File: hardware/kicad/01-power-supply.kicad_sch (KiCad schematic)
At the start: 29 parts, among them J1 USB_C, J3 JST PH 2-pin, Q1 SI2301CDS, SW16 SS-12D00G3, U2 IP5306, U3 SY8089AAAC, U4 USBLC6-2SC6

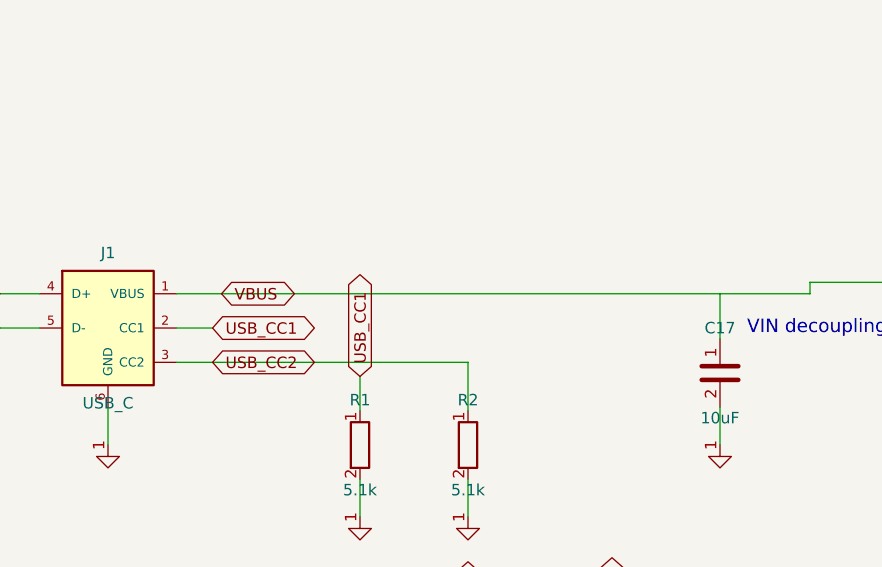
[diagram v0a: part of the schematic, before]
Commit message: feat(hw): EN RC network, fused VBUS input, current-limited backlight — R25 respin trio
Three coordinated design fixes landed together with their full gate,
bench and release integration (work split across two parallel sessions):

- R3 (10k) + C31 (100nF) on EN — the RC the module datasheet p.28
  fig.7 requires (R25-CRIT-1: every board through v4.3.1 shipped
  without it on the strength of a false justification comment).
  EN now solves to the +3V3 rail through the pull-up.
- F1 (PTC resettable fuse 2A 1812, C960026) on the USB input:
  J1 delivers on the new VBUS_IN net and reaches VBUS through F1.
  PWR_FLAG added on the post-fuse rail (J1's power-out pin moved nets).
- R27 (20R 1206) backlight series resistor: LED-A now fed from +5V
  through R27 on the new LED_BLA net (R25-HIGH-1, unbounded current).
  First placement collided with the LCD B.Cu verticals; final position
  (121.7, 45.5) clears the corridor.

Integration completed in this commit:
- verify_polarity: strict expectations for R3/C31/R27/F1, J1 pins moved
  to VBUS_IN, J4.8 backlight expectation moved to LED_BLA — all read
  off the copper.
- vbench corpus: R25-CRIT-1, R10-LOW-7, R25-HIGH-1 flipped from live
  board facts to mutation reinjection (detach R3/C31/R27 must be caught
  by name); R24-HIGH-3 moved to a move_pin drift mutation — the detach
  variant became structurally invisible to the bench once EN gained
  R3/C31 (declared-pad D3 exemption); note records why. usb_cold_boot
  flips its EN assertion exactly as its own text promised; export
  header now derives VB_EN_FLOATING=0; VBUS invariant follows the
  fused chain.
- Gates: R_1206/F_1812 footprints known, F1 value mapping, LED_BLA in
  the Net Explorer section law, schematic caption collisions resolved.
- Release fully synced (gerbers, BOM, CPL, d356, zip, jlcpcb mirror),
  iBOM + schematic SVG/PDF renders + combined PDF regenerated.

Tests: verify-all ALL CHECKS PASSED (incl. polarity 274 checks,
netlist-diff, isolation, e-test on release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
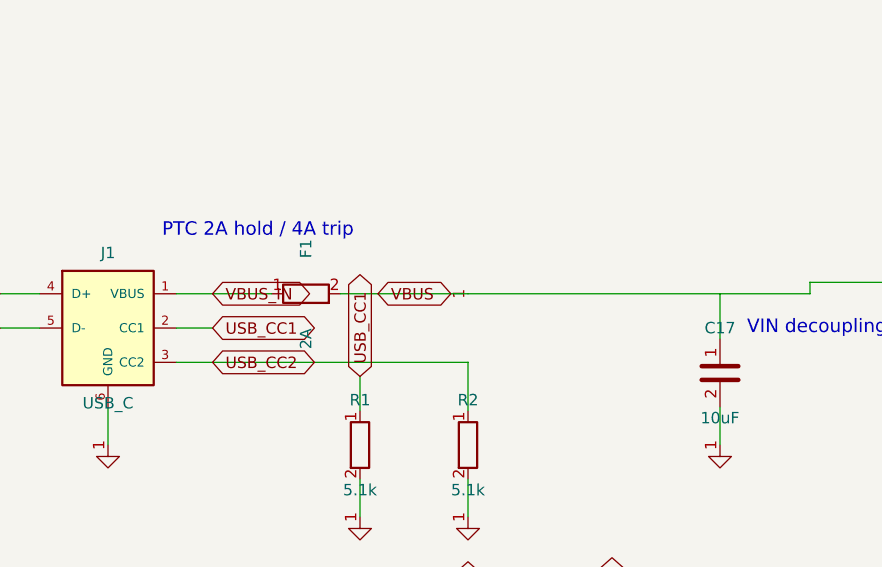
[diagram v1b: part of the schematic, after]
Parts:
- removed C18: 10uF, symbol C
- removed C19: 22uF, symbol C
- removed L2: 2.2uH, symbol L
- added C27: 10uF, symbol C
- added C30: 22uF, symbol C
- added F1: 2A, symbol R
- added R16: 100k, symbol R
- C18: renamed from R16; value 100k -> 10uF; symbol R -> C
- C19: renamed from C27; value 10uF -> 22uF
- L2: renamed from C30; value 22uF -> 2.2uH; symbol C -> L
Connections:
- net +3V3: now also C30.1
- net +5V: now also C19.1, C27.2, R16.1; no longer C18.1, C19.2
- net BAT+: now also C18.1
- net BUCK_LX: now also L2.2
- net GND: now also C18.2, C19.2, C27.1, C30.2; no longer C19.1, L2.2
- net IP5306_KEY: now also R16.2; no longer C18.2
- net VBUS: now also F1.2; no longer J1.1 (VBUS)
- new net VBUS_IN: F1.1, J1.1 (VBUS)
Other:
- note added: "PTC 2A hold / 4A trip"
- moved on the sheet: C19

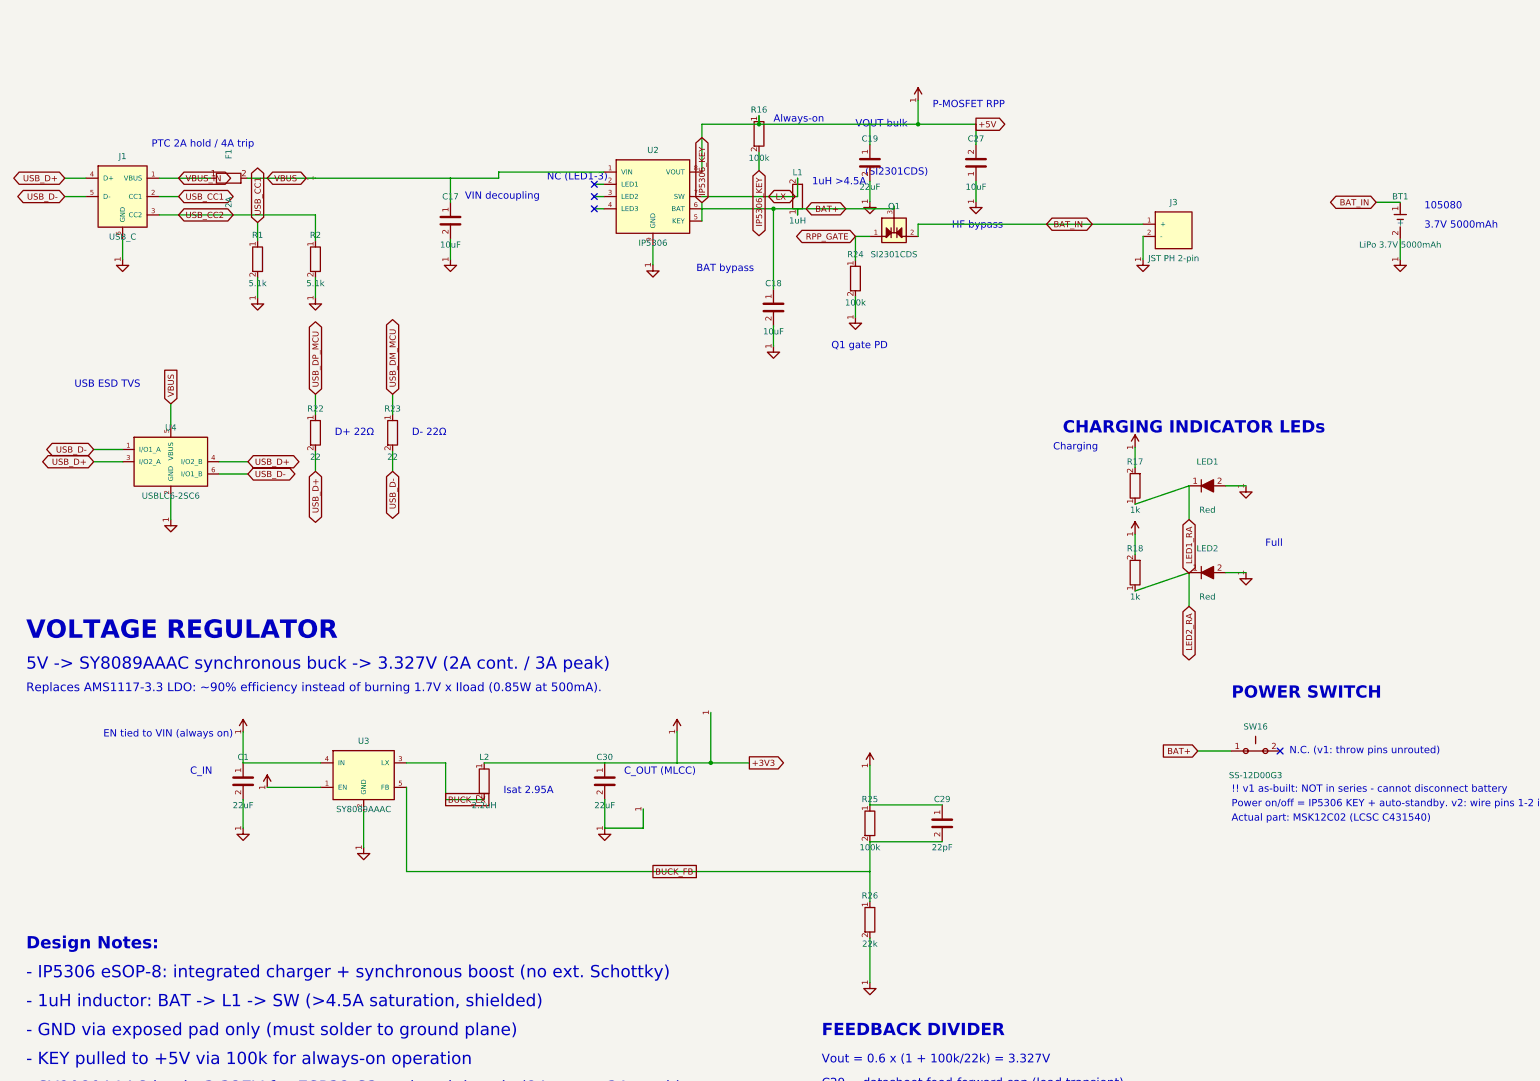
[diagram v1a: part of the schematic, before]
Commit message: feat(containment): layer 6 — ERC warning burn-down, 676 to ZERO, gate at all severities
Three root causes, three fixes in the schematic generator:

- 507 endpoint_off_grid: sheets lay out on a human 1 mm grid while KiCad
  connects on 1.27 mm. snap() in kicad_primitives now grid-snaps every
  connection-bearing coordinate at emission. Snapping is monotonic and
  distributes over the library's grid-multiple pin offsets, so points
  that coincided before still coincide after; zero-length stub wires
  that collapse onto their anchor are dropped.
- The stragglers came from three symbols whose pin connection points
  were themselves off-grid: BAT54C (±5.0 → ±5.08, top 5.0 → 5.08, used
  by D1 and Q1), USBLC6-2SC6 (±10.0 → ±10.16), Speaker (±0.635 →
  ±1.27). Their sheet wiring moved with them in the same commit.
- 169 lib_symbol_issues: bare lib_ids referenced library "" which no
  configuration includes. Symbols are now emu:<name>, resolved by a
  generated hardware/kicad/sym-lib-table + emu.kicad_sym built from the
  same SYMBOLS strings as the embedded caches — cache and library
  cannot disagree by construction.

verify_erc now runs --severity-all against a ZERO baseline: from zero,
any new warning is a regression a specific change introduced. The
website's per-sheet SVGs/PDFs are re-rendered, and the "Download all
sheets" PDF — a one-off hand merge nothing regenerated, stale since the
R25 respin — is now merged by render-schematics.sh from the exported
sheets.

Suite: 85/85 green; netlist_diff vs PCB confirms connectivity unchanged.

Co-Authored-By: Claude Fable 5 <noreply@anthropic.com>
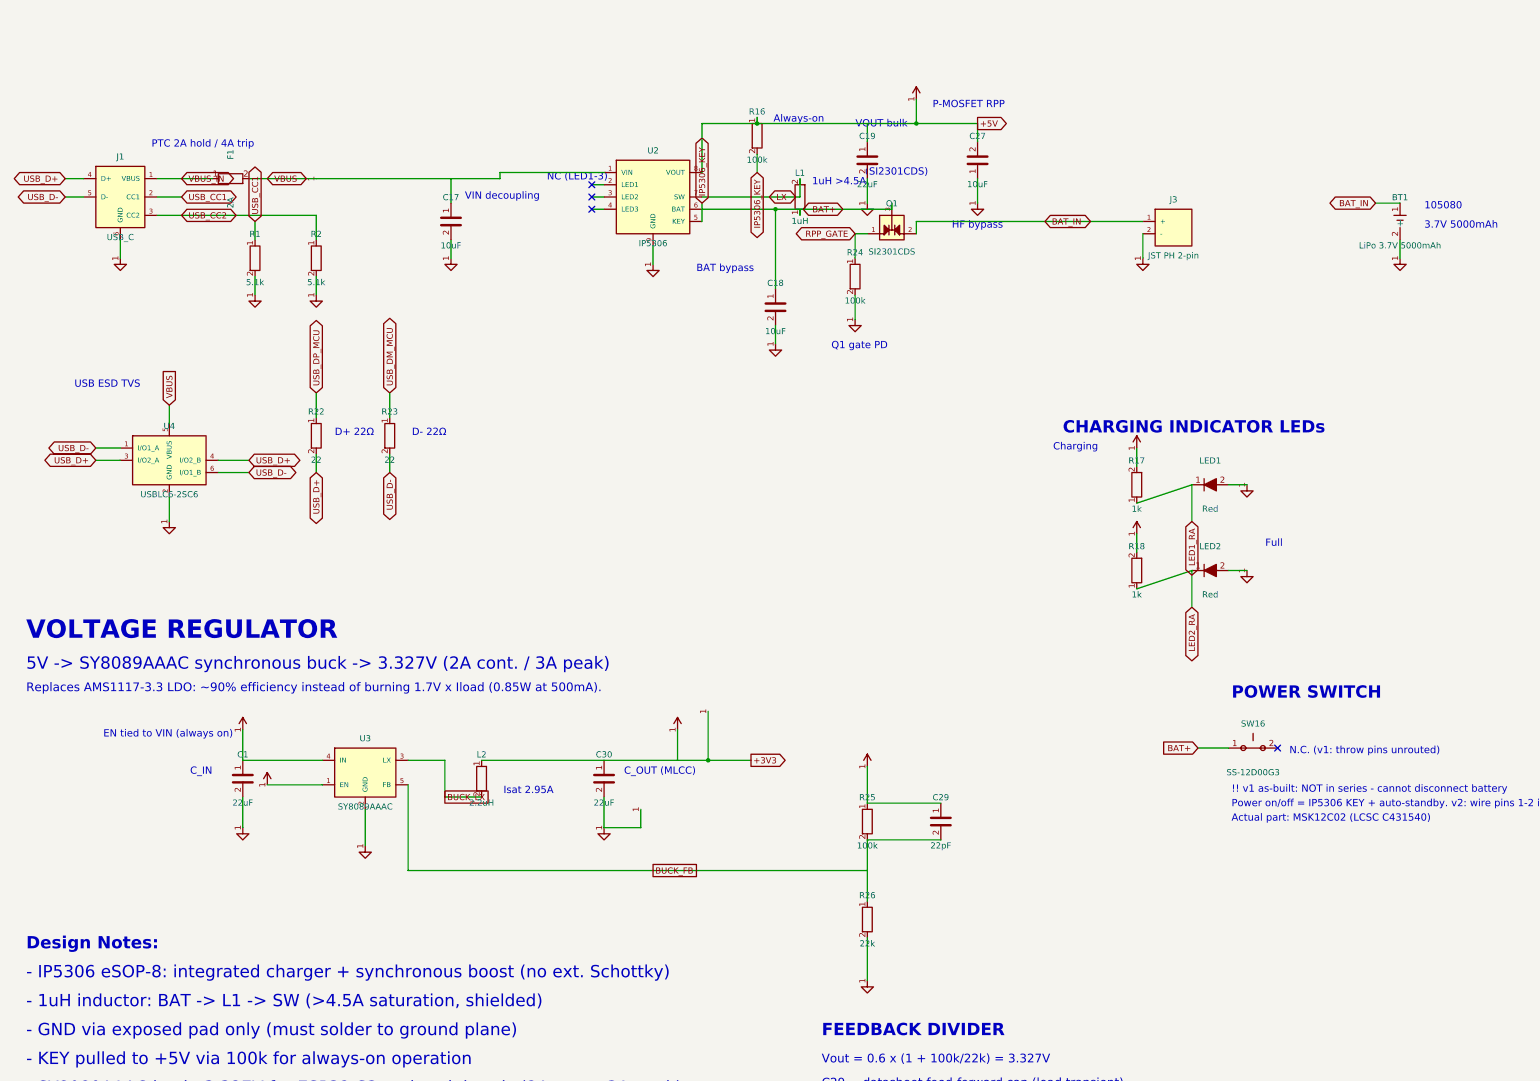
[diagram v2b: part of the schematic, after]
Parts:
- BT1: symbol Battery -> emu:Battery
- C1, C17, C18, C19, C27, C29, C30: symbol C -> emu:C
- F1, R1, R16, R17, R18, R2, R22, R23, R24, R25, R26: symbol R -> emu:R
- J1: symbol USB_C -> emu:USB_C
- J3: symbol Conn_JST_PH_2 -> emu:Conn_JST_PH_2
- L1, L2: symbol L -> emu:L
- LED1, LED2: symbol LED -> emu:LED
- Q1: symbol BAT54C -> emu:BAT54C
- SW16: symbol SW_Push -> emu:SW_Push
- U2: symbol IP5306 -> emu:IP5306
- U3: symbol SY8089AAAC -> emu:SY8089AAAC
- U4: symbol USBLC6_2SC6 -> emu:USBLC6_2SC6
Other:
- moved on the sheet: C1, C19, C27, C30, J3, L1, L2, LED1, LED2, Q1, R1, R16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
